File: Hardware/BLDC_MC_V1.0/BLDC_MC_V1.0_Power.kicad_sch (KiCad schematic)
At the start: 20 parts, among them U1 LMR51440SDRRR

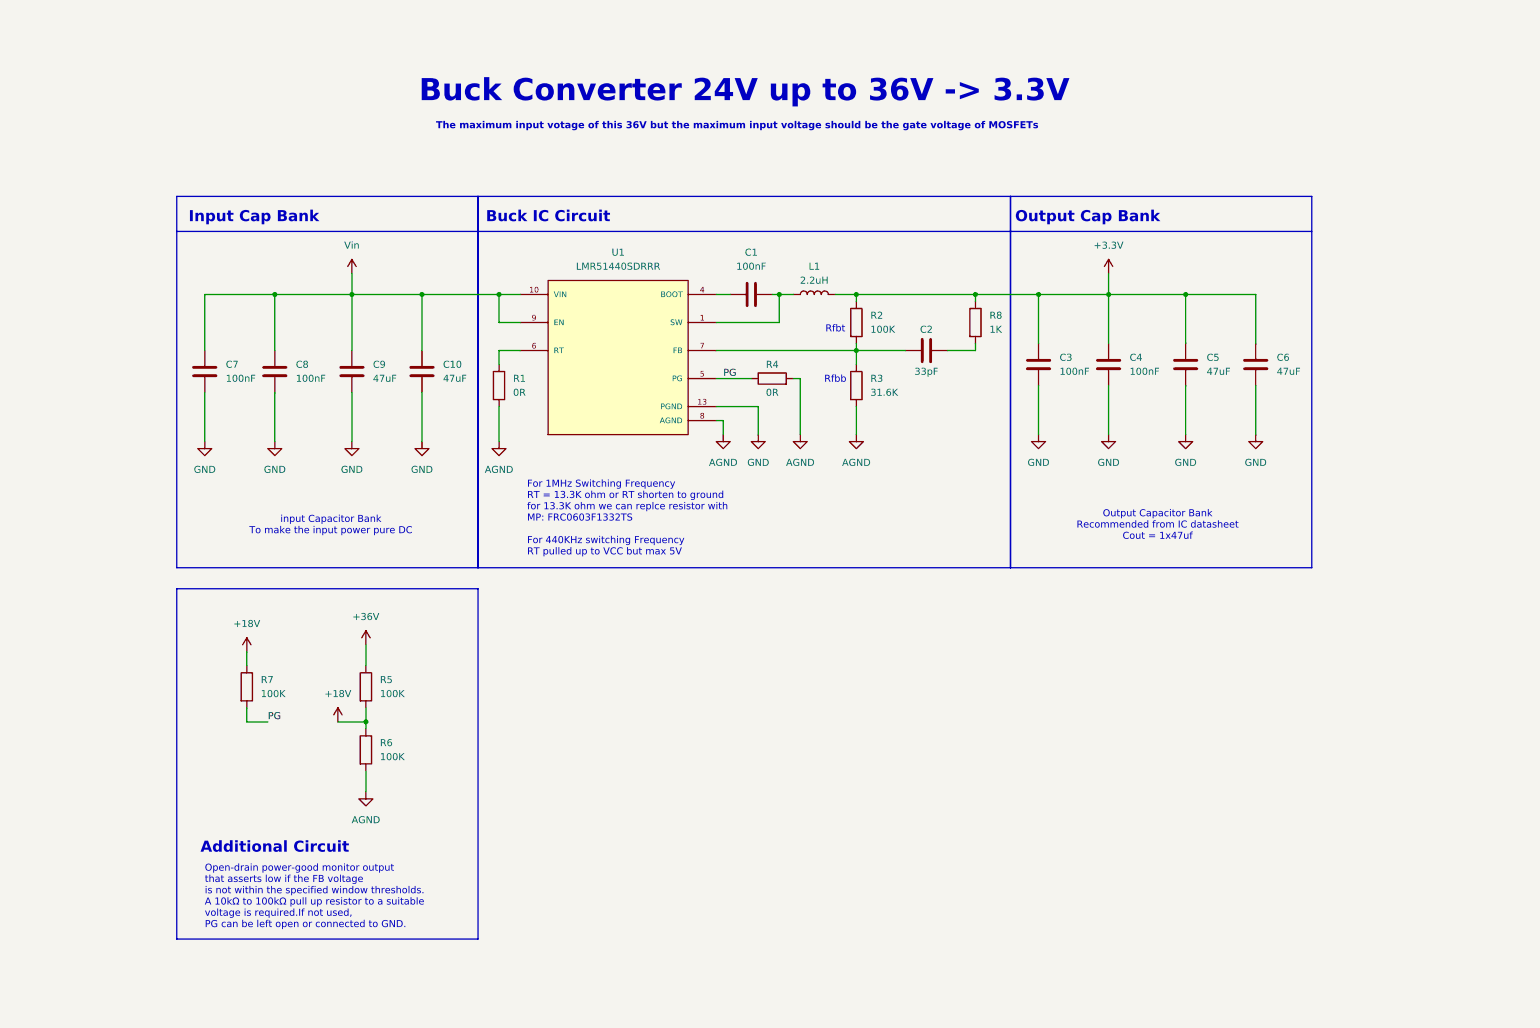
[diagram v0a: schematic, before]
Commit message: add the new edits to Buck converter sheet and edit other sheets name
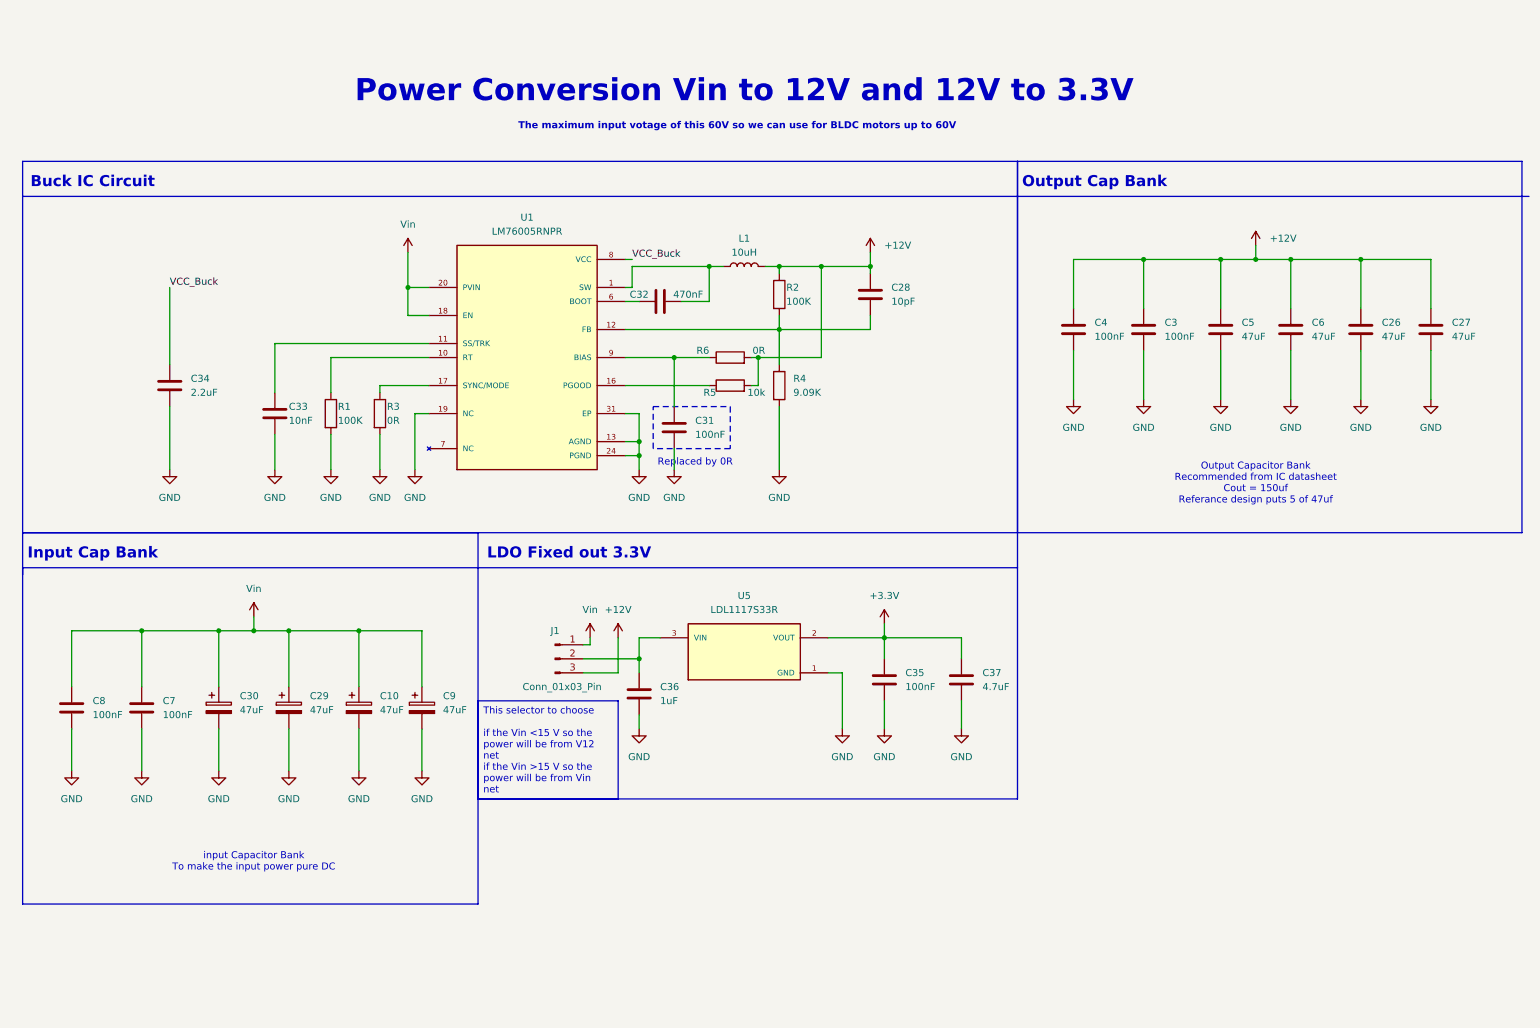
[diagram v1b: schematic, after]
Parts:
- removed C1: 100nF, Capacitor_SMD:C_0603_1608Metric, symbol Device:C
- removed C10, C9: 47uF, Capacitor_SMD:C_1206_3216Metric, symbol Device:C
- removed C2: 33pF, Capacitor_SMD:C_0603_1608Metric, symbol Device:C
- removed R7: 100K, Resistor_SMD:R_0603_1608Metric, symbol Device:R
- removed R8: 1K, Resistor_SMD:R_0603_1608Metric, symbol Device:R
- removed U1: LMR51440SDRRR, BLDC_Motor_Driver_Components_Footprint:CONV_LMR51440SDRRR, symbol LMR51440SDRRR:LMR51440SDRRR
- added C10, C29, C30, C9: 47uF, Capacitor_SMD:CP_Elec_10x10.5, symbol Device:C_Polarized
- added C26, C27: 47uF, Capacitor_SMD:C_1206_3216Metric, symbol Device:C
- added C28: 10pF, Capacitor_SMD:C_0603_1608Metric, symbol Device:C
- added C31, C35: 100nF, Capacitor_SMD:C_0805_2012Metric, symbol Device:C
- added C32: 470nF, Capacitor_SMD:C_0805_2012Metric, symbol Device:C
- added C33: 10nF, Capacitor_SMD:C_0603_1608Metric, symbol Device:C
- added C34: 2.2uF, Capacitor_SMD:C_0603_1608Metric, symbol Device:C
- added C36: 1uF, Capacitor_SMD:C_0805_2012Metric, symbol Device:C
- added C37: 4.7uF, Capacitor_SMD:C_1206_3216Metric, symbol Device:C
- added J1: Conn_01x03_Pin, Connector_PinHeader_2.54mm:PinHeader_1x03_P2.54mm_Vertical, symbol Connector:Conn_01x03_Pin
- added U1: LM76005RNPR, BLDC_Motor_Driver_Components_Footprint:QFN50P600X400X80-31N, symbol LM76005RNPR:LM76005RNPR
- added U5: LDL1117S33R, BLDC_Motor_Driver_Components_Footprint:SOT230P700X180-4N, symbol LDL1117S33R:LDL1117S33R
- C3, C4, C7, C8: footprint Capacitor_SMD:C_0603_1608Metric -> Capacitor_SMD:C_0805_2012Metric; LCSC_PN C1591 -> C28233; MP CL10B104KB8NNNC -> CL21B104KCFNNNE
- L1: value 2.2uH -> 10uH; footprint Inductor_SMD:L_TechFuse_SL0420 -> Inductor_SMD:L_KOHERelec_MDA7030; LCSC_PN C2847469 -> C149584; MP MDA4020-2R2M -> SMMS0650-100M
- R1: value 0R -> 100K; LCSC_PN C2906974 -> C14675; MP FRC0603F0000TS -> RC0603FR-07100KL
- R3: value 31.6K -> 0R; LCSC_PN C844551 -> C2906974; MP CRCW060331K6FKEA -> FRC0603F0000TS
- R4: value 0R -> 9.09K; LCSC_PN C2906974 -> C844591; MP FRC0603F0000TS -> CRCW06039K09FKEA
- R5: value 100K -> 10k; LCSC_PN C14675 -> C98220; MP RC0603FR-07100KL -> RC0603FR-0710KL
- R6: value 100K -> 0R; LCSC_PN C14675 -> C2906974; MP RC0603FR-07100KL -> FRC0603F0000TS
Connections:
- net +3.3V: now also C35.1, C37.1, U5.2 (VOUT), U5.4 (VOUT); no longer C3.2, C4.2, C5.2, C6.2, L1.2, R2.1
- net AGND: now also C3.2, C4.2, C5.1, C6.1, C7.2, C8.2, C10.2, C26.1, C27.1, C29.2, C30.2, C31.2, C33.2, C34.2, C35.2, C36.2, C37.2, C9.2, U1.13 (AGND), U1.14 (AGND), U1.15 (AGND), U1.19 (NC), U1.24 (PGND), U1.25 (PGND), U1.26 (PGND), U1.27 (NC), U1.28 (NC), U1.29 (NC), U1.30 (NC), U1.31 (EP), U5.1 (GND); no longer R6.2
- net Vin: now also C7.1, C8.1, C10.1, C29.1, C30.1, C9.1, J1.1 (Pin_1), U1.18 (EN), U1.20 (PVIN), U1.21 (PVIN), U1.22 (PVIN); no longer C7.2, C8.2
- net at R1.1: now also U1.10 (RT)
- net at L1.1: now also C32.1, U1.1 (SW), U1.2 (SW), U1.3 (SW), U1.4 (SW), U1.5 (SW)
- net at R3.1: now also U1.17 (SYNC/MODE); no longer R2.2
- net +18V: no longer names the net of R6.1
- net +18V: now also C31.1, U1.9 (BIAS); no longer R5.2
- net +36V: no longer names the net of R5.1
- net +36V: now also U1.16 (PGOOD)
- removed net GND: C3.1, C4.1, C5.1, C6.1, C7.1, C8.1
- net PG: no longer names the net of R4.1
- net PG: now also R2.2, C28.2, U1.12 (FB)
- new net: C36.1, J1.2 (Pin_2), U5.3 (VIN)
- new net: C33.1, U1.11 (SS/TRK)
- new net: U1.23 (NC), U1.7 (NC)
- new net: C32.2, U1.6 (BOOT)
- new net +12V: C26.2, C27.2, C28.1, C3.1, C4.1, C5.2, C6.2, J1.3 (Pin_3), L1.2, R2.1, R5.2, R6.2
- new net VCC_Buck: C34.1, U1.8 (VCC)
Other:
- note added: "LDO Fixed out 3.3V"
- note added: "Output Capacitor Bank Recommended from IC datasheet Cout = 150uf Referance design puts 5 of 47uf"
- note added: "Power Conversion Vin to 12V and 12V to 3.3V"
- note added: "Replaced by 0R"
- note added: "The maximum input votage of this 60V so we can use for BLDC motors up to 60V"
- note removed: "Additional Circuit"
- note removed: "Buck Converter 24V up to 36V -> 3.3V"
- note removed: "For 1MHz Switching Frequency RT = 13.3K ohm or RT shorten to ground for 13.3K ohm we can replce resistor with MP: FRC0603F1332TS For 440KHz switching Frequency RT pulled up to VCC but max 5V"
- note removed: "Open-drain power-good monitor output that asserts low if the FB voltage is not within the specified window thresholds. A 10kΩ to 100kΩ pull up resistor to a suitable voltage is required.If not used, PG can be left open or connected to GND."
- note removed: "Output Capacitor Bank Recommended from IC datasheet Cout = 1x47uf"
- note removed: "Rfbb"
- note removed: "Rfbt"
- note removed: "The maximum input votage of this 36V but the maximum input voltage should be the gate voltage of MOSFETs"
- moved on the sheet: C5, C6

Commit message: Add 5V LDO
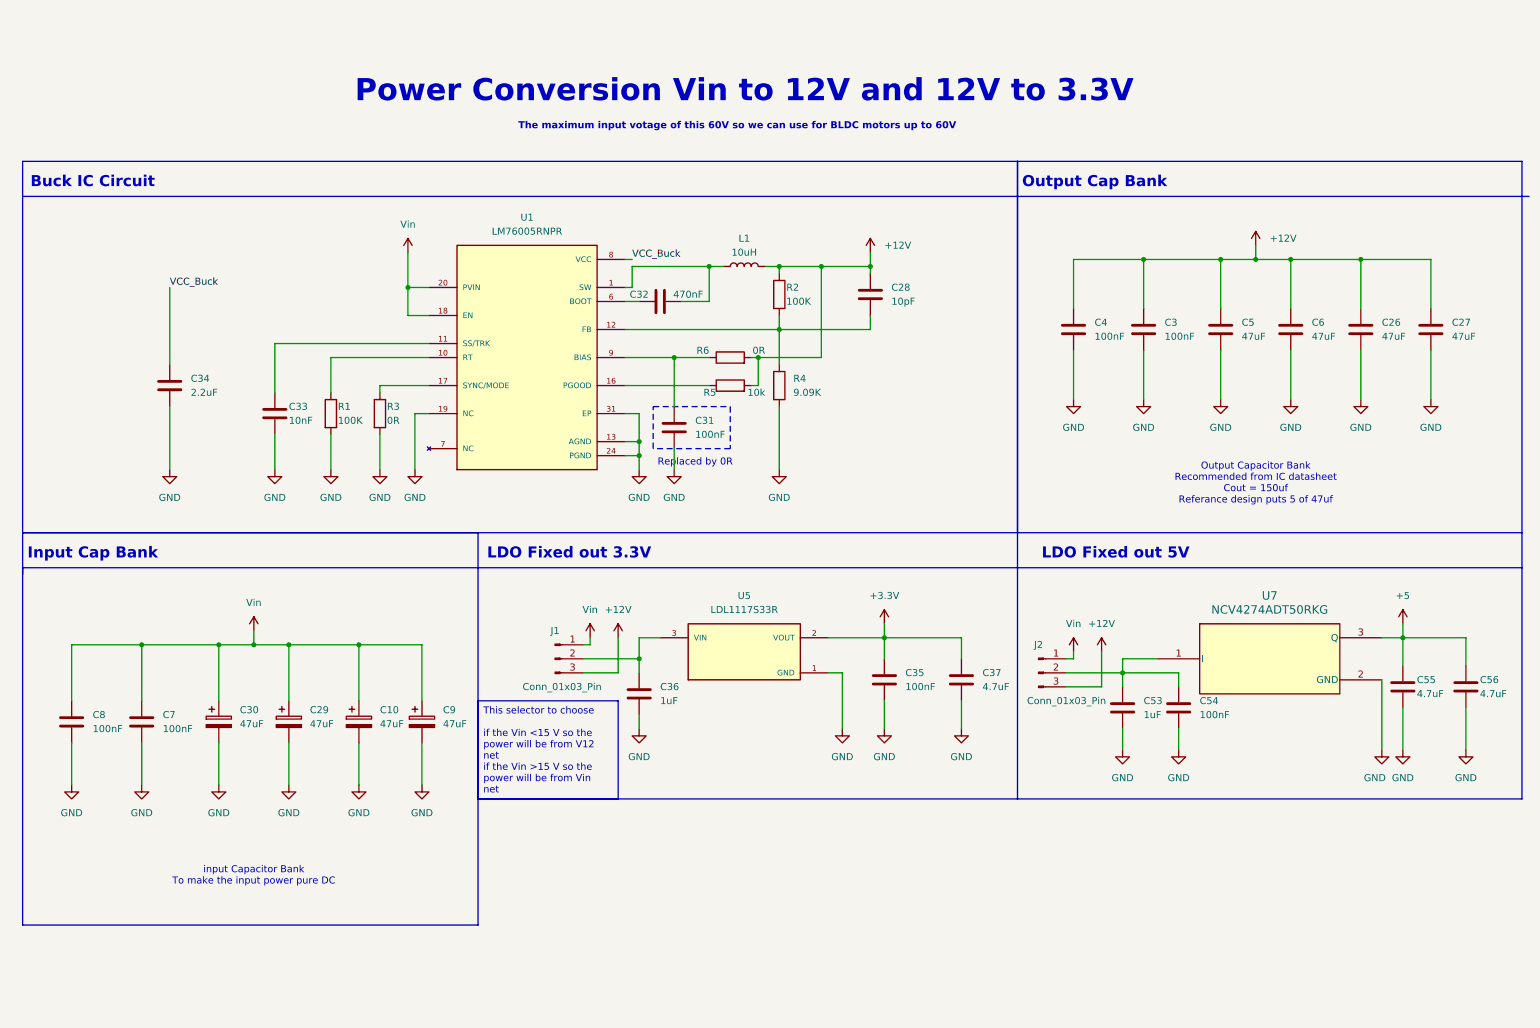
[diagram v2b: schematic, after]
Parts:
- added C53: 1uF, Capacitor_SMD:C_0805_2012Metric, symbol Device:C
- added C54: 100nF, Capacitor_SMD:C_0805_2012Metric, symbol Device:C
- added C55, C56: 4.7uF, Capacitor_SMD:C_1206_3216Metric, symbol Device:C
- added J2: Conn_01x03_Pin, Connector_PinHeader_2.54mm:PinHeader_1x03_P2.54mm_Vertical, symbol Connector:Conn_01x03_Pin
- added U7: NCV4274ADT50RKG, BLDC_Motor_Driver_Components_Footprint:DPAK-3_ONS, symbol NCV4274ADT50RKG:NCV4274ADT50RKG
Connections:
- net +12V: now also J2.3 (Pin_3)
- net AGND: now also C53.2, C54.2, C55.2, C56.2, U7.2 (GND)
- net Vin: now also J2.1 (Pin_1)
- new net: C53.1, C54.1, J2.2 (Pin_2), U7.1 (I)
- new net +5: C55.1, C56.1, U7.3 (Q)
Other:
- note added: "LDO Fixed out 5V"
- moved on the sheet: C10, C29, C30, C7, C8, C9

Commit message: Add the USB-C connector - define the PWM pins and other enable and fault pins for gate driver
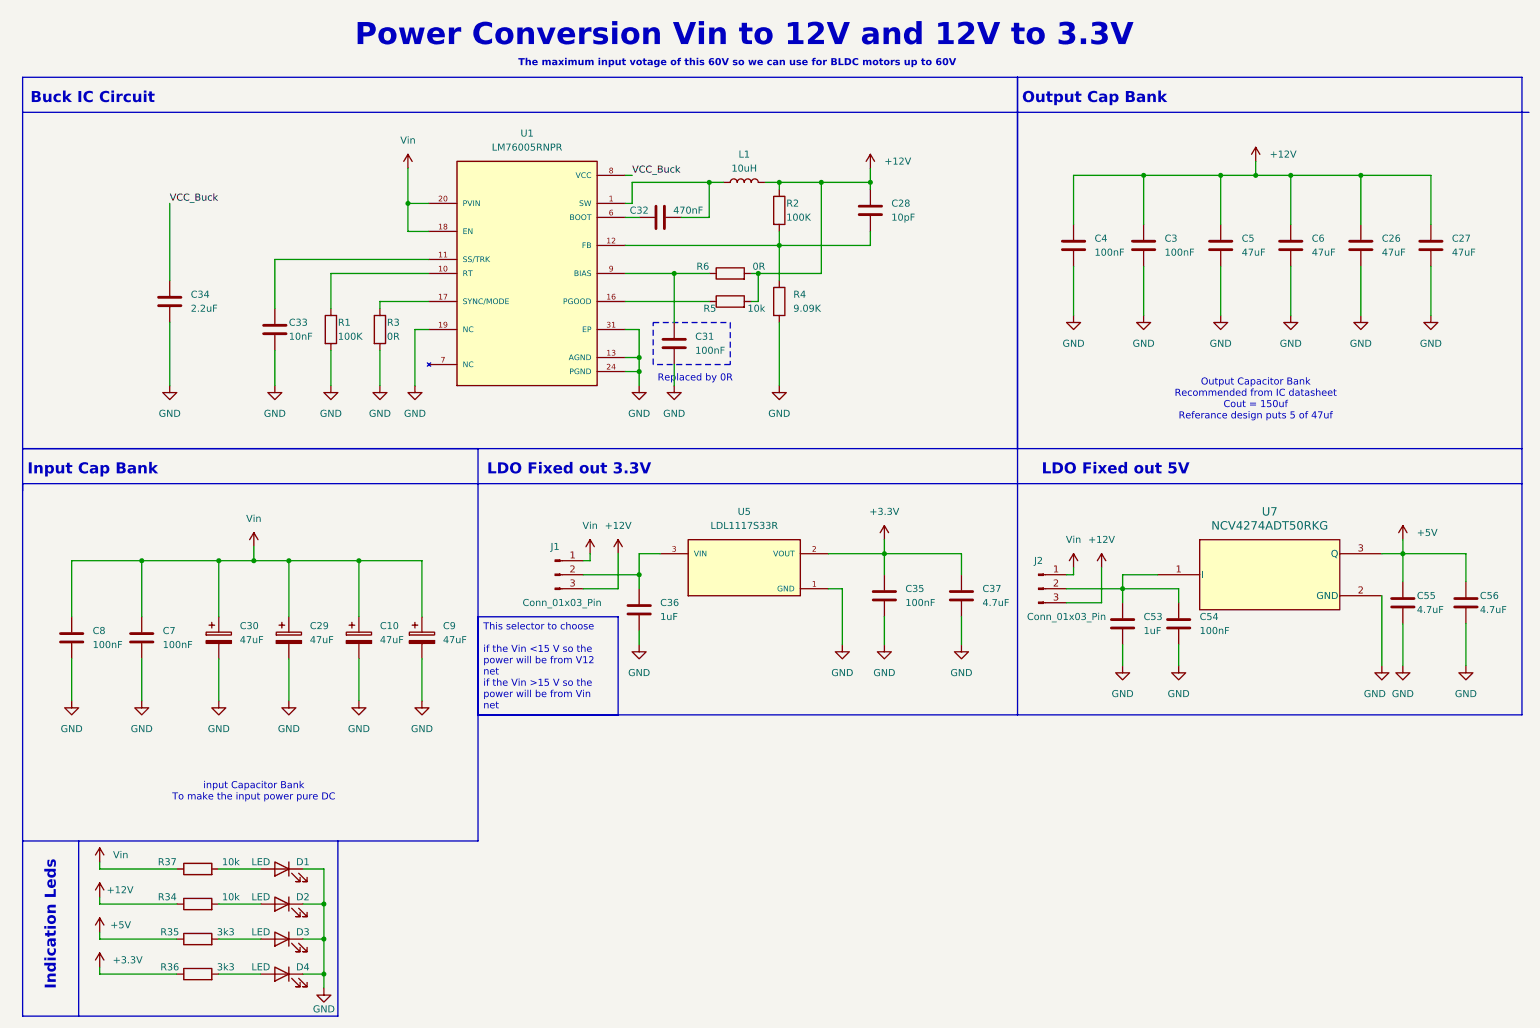
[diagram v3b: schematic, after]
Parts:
- added D1, D2, D3, D4: LED, LED_SMD:LED_0603_1608Metric, symbol Device:LED
- added R34, R37: 10k, Resistor_SMD:R_0603_1608Metric, symbol Device:R
- added R35, R36: 3k3, Resistor_SMD:R_0603_1608Metric, symbol Device:R
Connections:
- net +12V: now also R34.1
- net +3.3V: now also R36.1
- net AGND: now also D1.1 (K), D2.1 (K), D3.1 (K), D4.1 (K)
- net Vin: now also R37.1
- net +5 renamed +5V
- net +5V: now also R35.1
- new net: D1.2 (A), R37.2
- new net: D3.2 (A), R35.2
- new net: D4.2 (A), R36.2
- new net: D2.2 (A), R34.2
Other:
- note added: "Indication Leds"
- moved on the sheet: C10, C26, C27, C28, C29, C3, C30, C31, C32, C33, C34, C35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

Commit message: Add voltage sensor to measure the 3 phase voltage of inverter bridge
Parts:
- R1, R2: LCSC_PN C14675 -> C122538; MP RC0603FR-07100KL -> RT0603BRD07100KL
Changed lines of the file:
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@@
 	)
 	(symbol
+		(lib_id "Device:R")
+		(at 68.58 72.39 0)
+		(unit 1)
+		(exclude_from_sim no)
+		(in_bom yes)
+		(on_board yes)
+		(dnp no)
+		(property "Reference" "R1"
+			(at 69.85 71.12 0)
+			(effects
+				(font
+					(size 1.27 1.27)
+				)
+				(justify left)
+			)
+		)
+		(property "Value" "100K"
+			(at 69.85 73.66 0)
+			(effects
+				(font
+					(size 1.27 1.27)
+				)
+				(justify left)
+			)
+		)
+		(property "Footprint" "Resistor_SMD:R_0603_1608Metric"
+			(at 66.802 72.39 90)
+			(effects
+				(font
+					(size 1.27 1.27)
+				)
+				(hide yes)
+			)
+		)
+		(property "Datasheet" "https://www.lcsc.com/datasheet/C14675.pdf"
+			(at 68.58 72.39 0)
+			(effects
+				(font
+					(size 1.27 1.27)
+				)
+				(hide yes)
+			)
+		)
+		(property "Description" "Resistor"
+			(at 68.58 72.39 0)
+			(effects
+				(font
+					(size 1.27 1.27)
+				)
+				(hide yes)
+			)
+		)
+		(property "LCSC_PN" "C122538"
+			(at 68.58 72.39 0)
+			(effects
+				(font
+					(size 1.27 1.27)
+				)
+				(hide yes)
+			)
+		)
+		(property "MP" "RT0603BRD07100KL"
+			(at 68.58 72.39 0)
+			(effects
+				(font
+					(size 1.27 1.27)
+				)
+				(hide yes)
+			)
+		)
+		(property "Assembled" "Yes"
+			(at 68.58 72.39 0)
+			(effects
+				(font
+					(size 1.27 1.27)
+				)
+				(hide yes)
+			)
+		)
+		(pin "1"
+		)
+		(pin "2"
+		)
+		(instances
+			(project "BLDC_MC_V1.0"
+				(path "/e34fda66-7244-4ac9-bbf7-3725f03e688f/e7fbbff1-7265-43e4-97d7-cbbb02426874"
+					(reference "R1")
+					(unit 1)
+				)
+			)
+		)
+	)
+	(symbol
 		(lib_id "power:+3.3V")
 		(at 166.37 43.18 0)
@@
 	)
 	(symbol
-		(lib_id "Device:R")
-		(at 68.58 72.39 0)
-		(unit 1)
-		(exclude_from_sim no)
-		(in_bom yes)
-		(on_board yes)
-		(dnp no)
-		(property "Reference" "R1"
-			(at 69.85 71.12 0)
-			(effects
-				(font
-					(size 1.27 1.27)
-				)
-				(justify left)
-			)
-		)
-		(property "Value" "100K"
-			(at 69.85 73.66 0)
-			(effects
-				(font
-					(size 1.27 1.27)
-				)
-				(justify left)
-			)
-		)
-		(property "Footprint" "Resistor_SMD:R_0603_1608Metric"
-			(at 66.802 72.39 90)
-			(effects
-				(font
-					(size 1.27 1.27)
-				)
-				(hide yes)
-			)
-		)
-		(property "Datasheet" "https://www.lcsc.com/datasheet/C14675.pdf"
-			(at 68.58 72.39 0)
-			(effects
-				(font
-					(size 1.27 1.27)
-				)
-				(hide yes)
-			)
-		)
-		(property "Description" "Resistor"
-			(at 68.58 72.39 0)
-			(effects
-				(font
-					(size 1.27 1.27)
-				)
-				(hide yes)
-			)
-		)
-		(property "LCSC_PN" "C14675"
-			(at 68.58 72.39 0)
-			(effects
-				(font
-					(size 1.27 1.27)
-				)
-				(hide yes)
-			)
-		)
-		(property "MP" "RC0603FR-07100KL"
-			(at 68.58 72.39 0)
-			(effects
-				(font
-					(size 1.27 1.27)
-				)
-				(hide yes)
-			)
-		)
-		(property "Assembled" "Yes"
-			(at 68.58 72.39 0)
-			(effects
-				(font
-					(size 1.27 1.27)
-				)
-				(hide yes)
-			)
-		)
-		(pin "1"
-		)
-		(pin "2"
-		)
-		(instances
-			(project "BLDC_MC_V1.0"
-				(path "/e34fda66-7244-4ac9-bbf7-3725f03e688f/e7fbbff1-7265-43e4-97d7-cbbb02426874"
-					(reference "R1")
-					(unit 1)
-				)
-			)
-		)
-	)
-	(symbol
 		(lib_id "Device:C")
 		(at 130.81 74.93 0)
@@
 			)
 		)
-		(property "LCSC_PN" "C14675"
+		(property "LCSC_PN" "C122538"
 			(at 149.86 50.8 0)
 			(effects
@@
 			)
 		)
-		(property "MP" "RC0603FR-07100KL"
+		(property "MP" "RT0603BRD07100KL"
 			(at 149.86 50.8 0)
 			(effects
